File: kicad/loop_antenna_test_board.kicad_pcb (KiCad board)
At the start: 2 copper layers, 0 parts

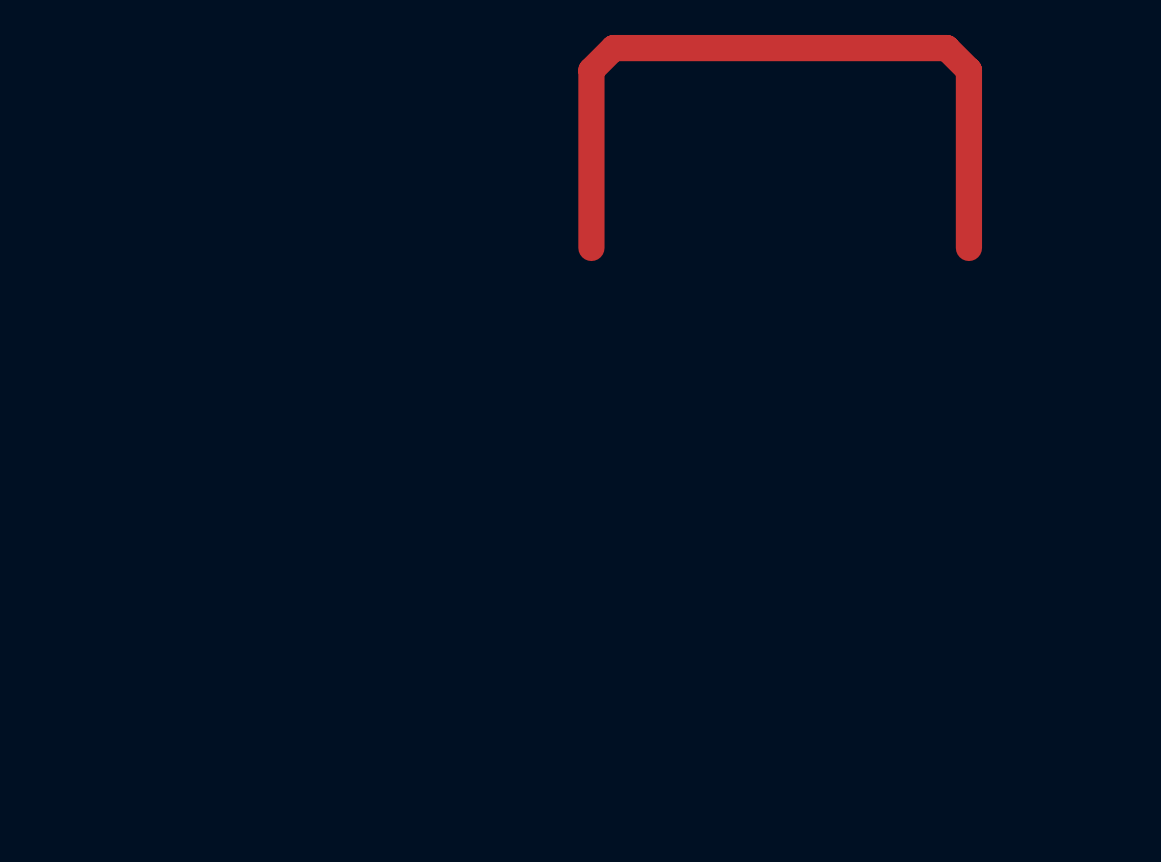
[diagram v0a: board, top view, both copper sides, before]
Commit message: added board layout
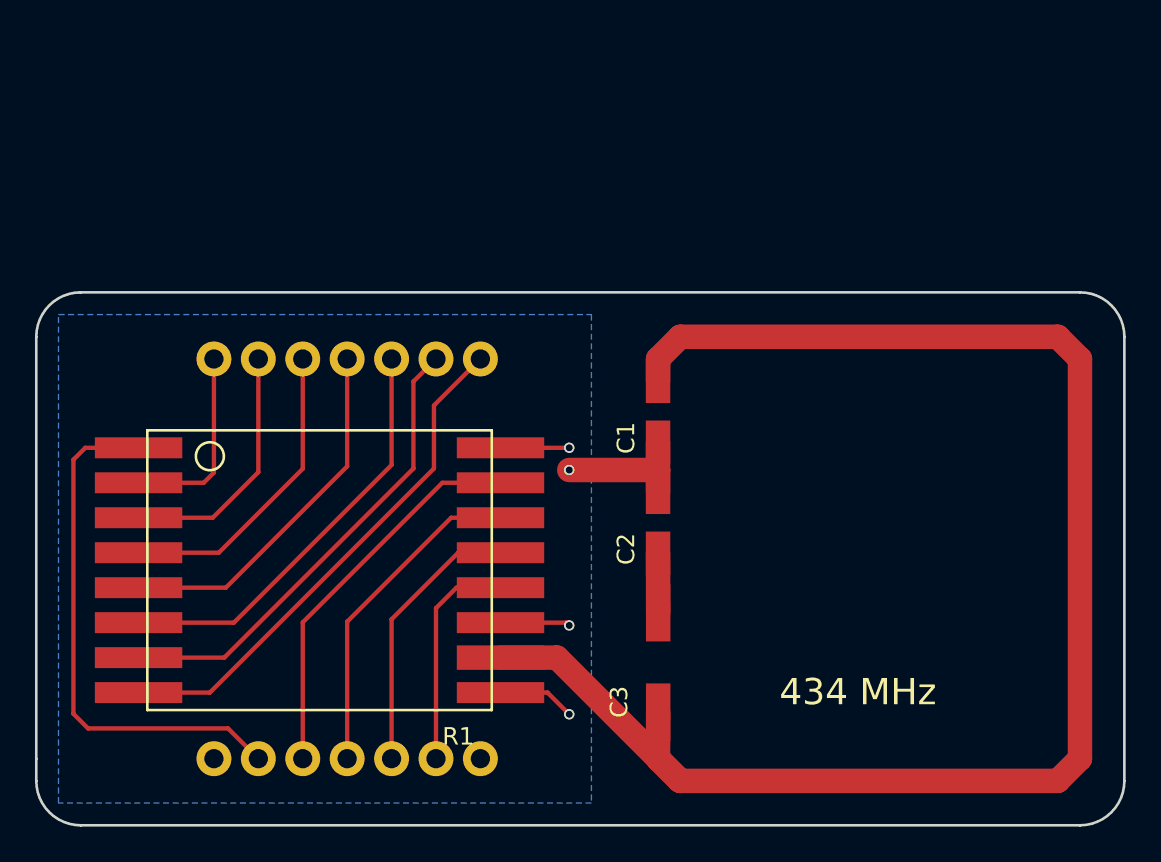
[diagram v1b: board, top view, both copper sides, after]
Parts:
- added C1: C, CAP, F.Cu at (161.3, 104.1)
- added C2: C, loop_antenna_test_board:CAP, F.Cu at (161.3, 110.5)
- added C3: CTRIM, loop_antenna_test_board:CAP_TUNABLE, F.Cu at (161.3, 117.4)
- added R1: RFM69W, loop_antenna_test_board:RFM69W, F.Cu at (132.1, 108.0)
- added R2: RFM69W_BB, RFM69W_BB, B.Cu at (143.5, 113.0)
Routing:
- net Net-(C1-Pad1): track 0.00 -> 90.3 mm
- net (no net): track 43.0 -> 0.00 mm
- net Net-(R1-Pad1): track 0.00 -> 30.2 mm
- net +3V3: track 0.00 -> 29.6 mm
- net /DIO5: track 0.00 -> 27.0 mm
- net /DIO4: track 0.00 -> 24.3 mm
- net Net-(R1-Pad15): track 0.00 -> 22.4 mm
- net /DIO3: track 0.00 -> 20.9 mm
- net GND: track 0.00 -> 20.7 mm, vias 0 -> 4
- net /MOSI: track 0.00 -> 19.1 mm
- net /DIO2: track 0.00 -> 17.7 mm
- net /MISO: track 0.00 -> 15.8 mm
- net /DIO1: track 0.00 -> 14.4 mm
- net /SCK: track 0.00 -> 12.8 mm
- net /DIO0: track 0.00 -> 11.0 mm
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- added copper zone on B.Cu, net GND
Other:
- board outline added: 62.2 x 30.5 mm
- board text added: "434 MHz"
- board text added: "LOOP ANTENNA TEST BOARD V 1.0.0"
- board text added: "hochreiner.net"

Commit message: changed pcb layout
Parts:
- moved C3 1.39 mm to (160.0, 116.8)
- moved C1 1.27 mm to (160.0, 104.1)
- moved C2 1.27 mm to (160.0, 110.5)
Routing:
- net Net-(C1-Pad1): track 90.3 -> 92.6 mm
- net GND: track 20.7 -> 19.0 mm
- net /DIO1: track 14.4 -> 15.3 mm
- net Net-(C2-Pad2): track 3.39 -> 2.85 mm
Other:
- board size 62.2 x 30.5 mm -> 59.7 x 27.9 mm
- net class Default: clearance 0.2 -> 0.1524; trace_width 0.25 -> 0.254; via_dia 0.6 -> 0.6858; via_drill 0.4 -> 0.3302
- rule trace_clearance: 0.2 -> 0.1524
- rule trace_min: 0.2 -> 0.254
- rule via_min_drill: 0.3 -> 0.3302
- rule via_min_size: 0.4 -> 0.6858
- board text added: "3V3"
- board text added: "DIO0"
- board text added: "DIO1"
- board text added: "DIO2"
- board text added: "DIO3"
- board text added: "DIO4"
- board text added: "DIO5"
- board text added: "GND"
- board text added: "MISO"
- board text added: "MOSI"
- board text added: "NSS"
- board text added: "RESET"
- board text added: "SCK"

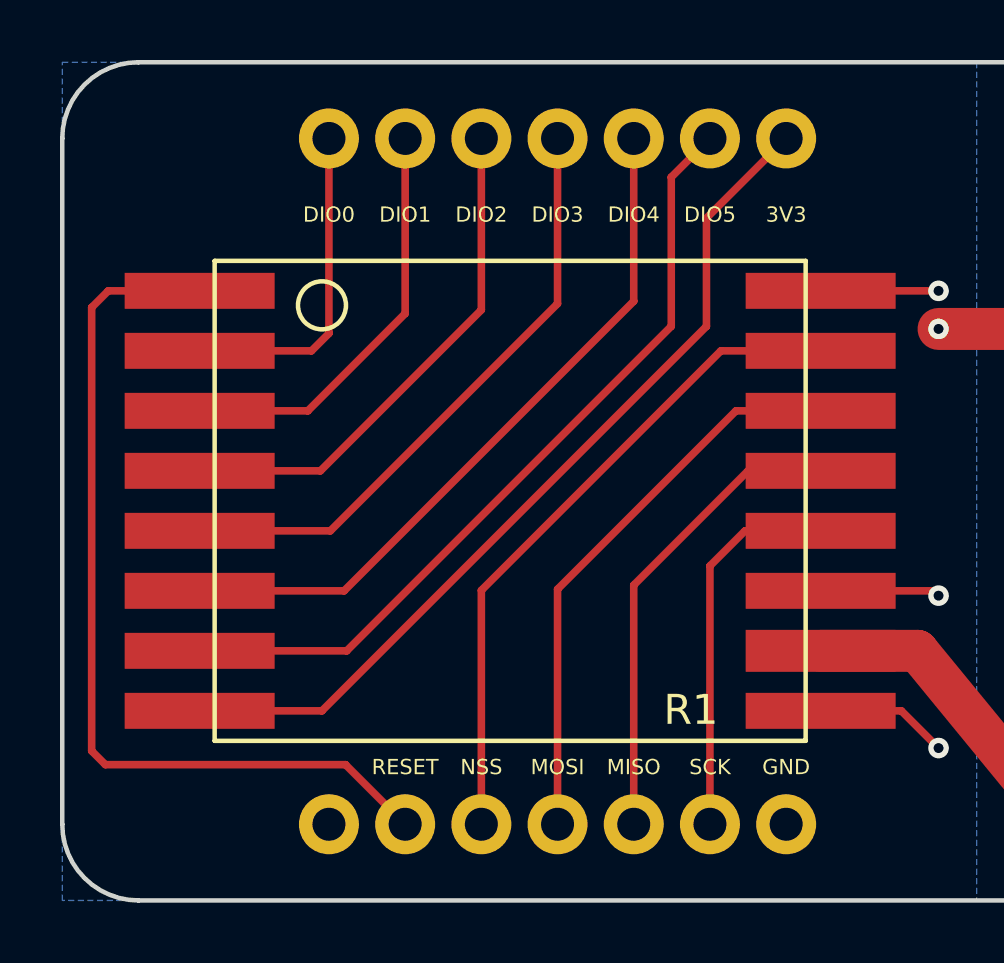
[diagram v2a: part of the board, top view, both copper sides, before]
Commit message: rerouted pbc and generated gerbers
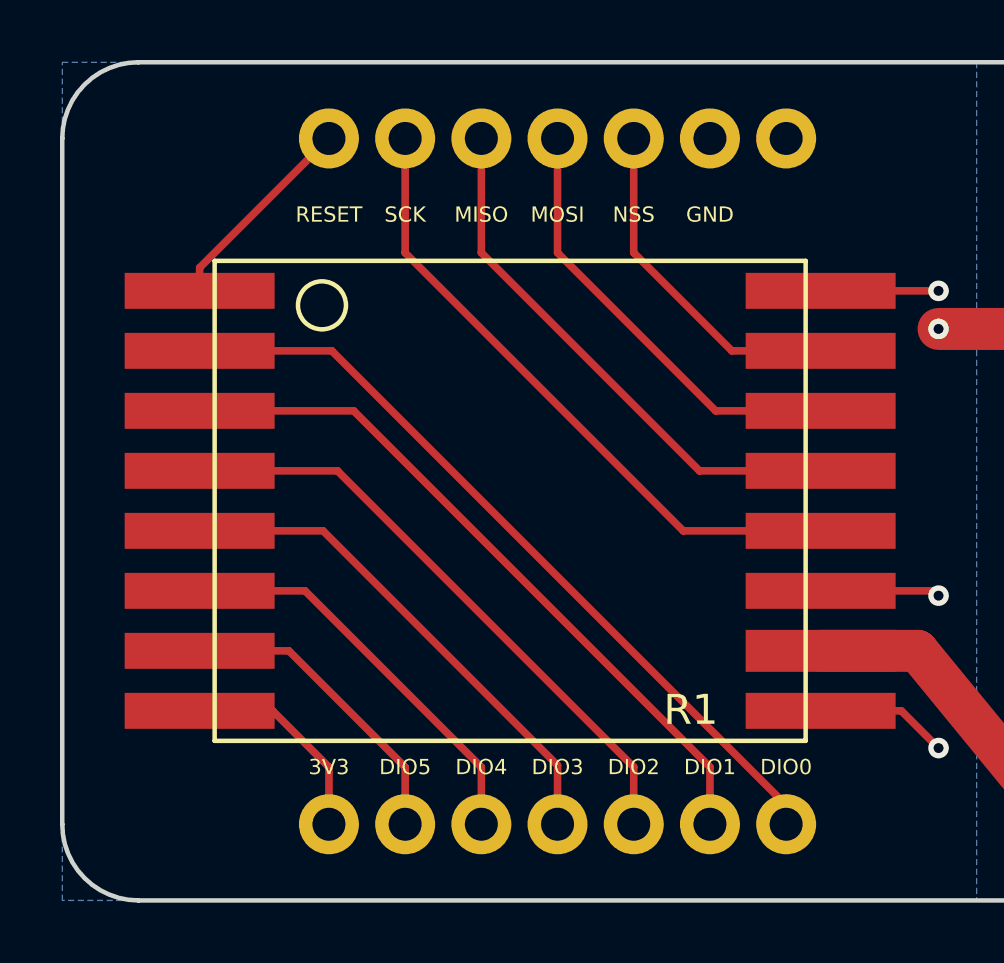
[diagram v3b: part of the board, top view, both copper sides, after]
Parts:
- moved R2 2.54 mm to (143.5, 115.6), turned to 180 degrees
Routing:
- net Net-(R1-Pad1): track 30.1 -> 6.87 mm
- net +3V3: track 29.6 -> 6.99 mm
- net /DIO5: track 27.0 -> 10.4 mm
- net /DIO0: track 11.0 -> 26.5 mm
- net Net-(R1-Pad15): track 22.4 -> 11.4 mm
- net /DIO4: track 23.9 -> 13.7 mm
- net /SCK: track 12.8 -> 21.5 mm
- net /DIO1: track 15.3 -> 23.8 mm
- net /MISO: track 15.8 -> 22.7 mm
- net /DIO3: track 20.6 -> 17.1 mm
- net /DIO2: track 17.3 -> 20.5 mm
- net /MOSI: track 19.1 -> 16.4 mm
